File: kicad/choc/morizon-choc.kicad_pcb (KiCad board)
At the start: 2 copper layers, 252 x 85 mm, 145 parts, among them SW1 SW_Push, SW10 SW_Push, SW11 SW_Push, SW12 SW_Push, SW13 SW_Push, SW14 SW_Push, SW15 SW_Push, SW16 SW_Push, SW17 SW_Push, SW18 SW_Push, SW19 SW_Push, SW2 SW_Push, SW20 SW_Push, SW21 SW_Push, SW22 SW_Push, SW23 SW_Push, SW24 SW_Push, SW25 SW_Push, SW26 SW_Push, SW27 SW_Push, SW28 SW_Push, SW29 SW_Push, SW3 SW_Push, SW30 SW_Push, SW31 SW_Push, SW32 SW_Push, SW33 SW_Push, SW34 SW_Push, SW35 SW_Push, SW36 SW_Push, SW37 SW_Push, SW38 SW_Push, SW39 SW_Push, SW4 SW_Push, SW40 SW_Push, SW41 SW_Push, SW42 SW_Push, SW43 SW_Push, SW44 SW_Push, SW45 SW_Push, SW46 SW_Push, SW47 SW_Push, SW48 SW_Push, SW49 SW_Push, SW5 SW_Push, SW50 SW_Push, SW51 SW_Push, SW52 SW_Push, SW53 SW_Push, SW54 SW_Push, SW55 SW_Push, SW56 SW_Push, SW57 SW_Push, SW58 SW_Push, SW59 SW_Push, SW6 SW_Push, SW60 SW_Push, SW61 SW_Push, SW62 SW_Push, SW63 SW_Push, SW64 SW_Push, SW65 SW_Push, SW66 SW_Push, SW7 SW_Push, SW8 SW_Push, SW9 SW_Push, U1 PRO-MICRO

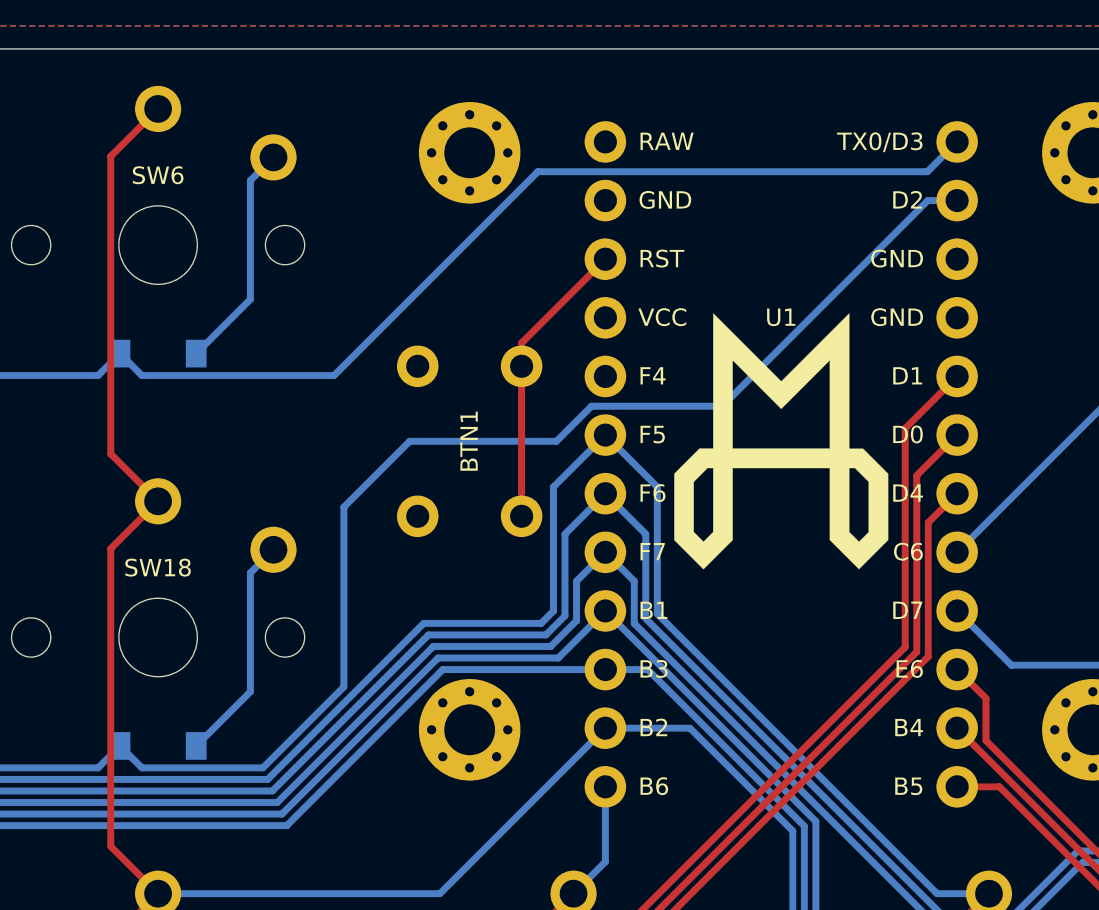
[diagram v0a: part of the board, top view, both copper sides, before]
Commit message: Implement Morizon MX
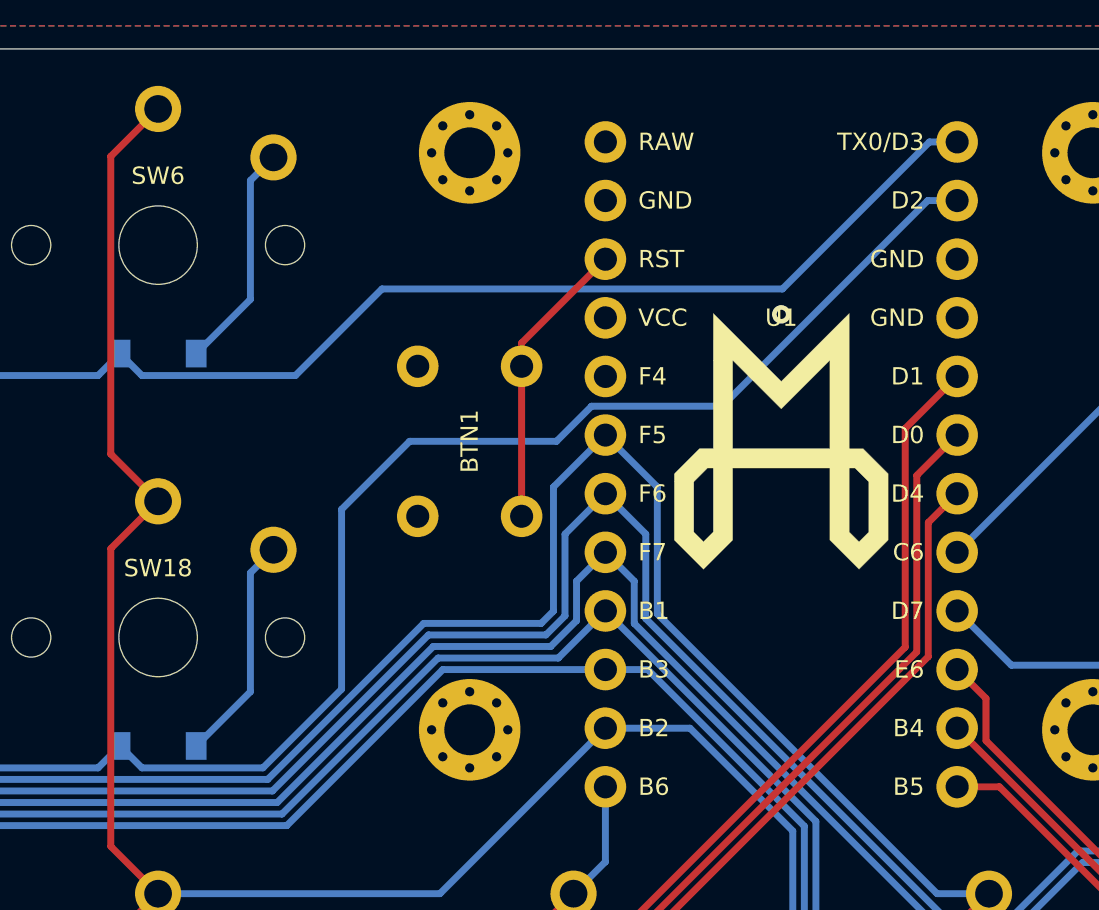
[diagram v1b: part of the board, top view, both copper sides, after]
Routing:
- net GND: vias 0 -> 1

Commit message: Upgrade project files to KiCad 6
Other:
- net class Default removed
- net class Power removed
- board text added: "rev1.1 | Choc"
- board text removed: "rev1 | Choc"

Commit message: Upgrade project files to KiCad 7
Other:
- board text added: "rev1.2 | Choc"
- board text removed: "rev1.1 | Choc"
